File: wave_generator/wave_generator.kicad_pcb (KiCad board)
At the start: 4 copper layers, 100 x 65 mm, 0 parts

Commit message: PCB not finished yet
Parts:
- added C1: 33uF, Capacitor_SMD:CP_Elec_6.3x5.9, F.Cu at (124.5, 72.0)
- added C10: 10uF, Capacitor_SMD:C_0603_1608Metric, F.Cu at (166.2, 73.0)
- added C11: 10uF, Capacitor_SMD:C_0603_1608Metric, F.Cu at (179.2, 74.8)
- added C12: 2.2uF, Capacitor_SMD:C_0603_1608Metric, F.Cu at (181.9, 74.8)
- added C13: 103, Capacitor_SMD:C_0603_1608Metric, F.Cu at (110.7, 96.5)
- added C14: 104, Capacitor_SMD:C_0603_1608Metric, F.Cu at (112.8, 96.5)
- added C15: 104, Capacitor_SMD:C_0603_1608Metric, F.Cu at (130.5, 103.5)
- added C16: 103, Capacitor_SMD:C_0603_1608Metric, F.Cu at (110.7, 110.0)
- added C17: 104, Capacitor_SMD:C_0603_1608Metric, F.Cu at (112.9, 110.0)
- added C18: 104, Capacitor_SMD:C_0603_1608Metric, F.Cu at (130.6, 118.9)
- added C19: 103, Capacitor_SMD:C_0603_1608Metric, F.Cu at (136.6, 103.5)
- added C2: 22uF, Capacitor_SMD:CP_Elec_6.3x5.9, F.Cu at (116.5, 72.0)
- added C20: 103, Capacitor_SMD:C_0603_1608Metric, F.Cu at (137.1, 118.9)
- added C21: 104, Capacitor_SMD:C_0603_1608Metric, F.Cu at (139.8, 100.2)
- added C22: 10pF, Capacitor_SMD:C_0603_1608Metric, F.Cu at (156.1, 100.7)
- added C23: 10pF, Capacitor_SMD:C_0603_1608Metric, F.Cu at (148.4, 100.7)
- added C24: 103, Capacitor_SMD:C_0603_1608Metric, F.Cu at (160.8, 111.8)
- added C25: 104, Capacitor_SMD:C_0603_1608Metric, F.Cu at (162.9, 111.8)
- added C26: 10uF, Capacitor_SMD:C_0603_1608Metric, F.Cu at (165.8, 111.0)
- added C27: 10uF, Capacitor_SMD:C_0603_1608Metric, F.Cu at (175.7, 101.3)
- added C28: 103, Capacitor_SMD:C_0603_1608Metric, F.Cu at (188.4, 113.7)
- added C29: 103, Capacitor_SMD:C_0603_1608Metric, F.Cu at (192.7, 88.9)
- added C3: 33uF, Capacitor_SMD:CP_Elec_6.3x5.9, F.Cu at (151.9, 75.0)
- added C30: 103, Capacitor_SMD:C_0603_1608Metric, F.Cu at (189.1, 89.0)
- added C31: 103, Capacitor_SMD:C_0603_1608Metric, F.Cu at (185.8, 89.0)
- added C32: 103, Capacitor_SMD:C_0603_1608Metric, F.Cu at (182.5, 89.0)
- added C33: 103, Capacitor_SMD:C_0603_1608Metric, F.Cu at (179.3, 89.0)
- added C34: 104, Capacitor_SMD:C_0603_1608Metric, F.Cu at (192.6, 84.1)
- added C35: 104, Capacitor_SMD:C_0603_1608Metric, F.Cu at (188.8, 84.0)
- added C36: 104, Capacitor_SMD:C_0603_1608Metric, F.Cu at (185.6, 84.1)
- added C37: 104, Capacitor_SMD:C_0603_1608Metric, F.Cu at (182.2, 84.1)
- added C38: 104, Capacitor_SMD:C_0603_1608Metric, F.Cu at (179.1, 84.1)
- added C4: 22uF, Capacitor_SMD:CP_Elec_6.3x5.9, F.Cu at (160.4, 75.0)
- added C5: 33uF, Capacitor_SMD:CP_Elec_6.3x5.9, F.Cu at (116.5, 86.5)
- added C6: 22uF, Capacitor_SMD:CP_Elec_6.3x5.9, F.Cu at (124.5, 86.5)
- added C7: 33uF, Capacitor_SMD:CP_Elec_6.3x5.9, F.Cu at (160.5, 86.5)
- added C8: 22uF, Capacitor_SMD:CP_Elec_6.3x5.9, F.Cu at (152.0, 86.5)
- added C9: 2.2uF, Capacitor_SMD:C_0603_1608Metric, F.Cu at (166.2, 77.0)
- added D1: LED_RED, LED_SMD:LED_0603_1608Metric, F.Cu at (184.3, 74.8)
- added D2: LED_BLUE, LED_SMD:LED_0603_1608Metric, F.Cu at (179.9, 128.0)
- added D3: LED_BLUE, LED_SMD:LED_0603_1608Metric, F.Cu at (179.8, 124.7)
- added F1: Fuse, Fuse:Fuse_1206_3216Metric, F.Cu at (111.0, 74.5)
- added F2: Fuse, Fuse:Fuse_1206_3216Metric, F.Cu at (111.0, 87.8)
- added J1: KF301_3PIN_POWER, myfootprint:KF301-3P, F.Cu at (103.2, 85.0)
- added J2: KF301_2PIN_INPUT, myfootprint:KF301-2P, F.Cu at (103.2, 100.0)
- added J3: KF301_2PIN_INPUT, myfootprint:KF301-2P, F.Cu at (103.2, 112.5)
- added J4: KF301_2PIN_OUTPUT, myfootprint:KF301-2P, F.Cu at (196.8, 97.3)
- added J5: UART, Connector_PinHeader_2.54mm:PinHeader_1x04_P2.54mm_Vertical, F.Cu at (167.4, 127.7)
- added J6: SWD, Connector_PinHeader_2.54mm:PinHeader_1x04_P2.54mm_Vertical, F.Cu at (152.2, 127.7)
- added J7: TEST, Connector_PinHeader_2.54mm:PinHeader_1x04_P2.54mm_Vertical, F.Cu at (137.6, 127.6)
- added R1: 200R, Resistor_SMD:R_0603_1608Metric, F.Cu at (114.9, 96.5)
- added R11: 10K, Resistor_SMD:R_0603_1608Metric, F.Cu at (115.1, 118.8)
- added R12: 10K, Resistor_SMD:R_0603_1608Metric, F.Cu at (132.8, 118.9)
- added R13: 30K, Resistor_SMD:R_0603_1608Metric, F.Cu at (134.9, 118.9)
- added R14: 10K, Resistor_SMD:R_0603_1608Metric, F.Cu at (141.2, 114.8)
- added R15: 10K, Resistor_SMD:R_0603_1608Metric, F.Cu at (139.8, 96.2)
- added R16: 1M, Resistor_SMD:R_0603_1608Metric, F.Cu at (152.5, 97.6)
- added R17: 10K, Resistor_SMD:R_0603_1608Metric, F.Cu at (169.4, 111.0)
- added R18: 10K, Resistor_SMD:R_0603_1608Metric, F.Cu at (160.8, 103.2)
- added R19: 10K, Resistor_SMD:R_0603_1608Metric, F.Cu at (175.6, 97.7)
- added R2: 200R, Resistor_SMD:R_0603_1608Metric, F.Cu at (117.0, 96.5)
- added R20: 10K, Resistor_SMD:R_0603_1608Metric, F.Cu at (180.1, 111.0)
- added R21: 30K, Resistor_SMD:R_0603_1608Metric, F.Cu at (184.9, 111.7)
- added R22: 300R, Resistor_SMD:R_0603_1608Metric, F.Cu at (188.4, 111.7)
- added R23: 10K, Resistor_SMD:R_0603_1608Metric, F.Cu at (191.7, 112.8)
- added R24: 3.3K, Resistor_SMD:R_0603_1608Metric, F.Cu at (188.0, 74.5)
- added R25: 3.3K, Resistor_SMD:R_0603_1608Metric, F.Cu at (185.4, 128.0)
- added R26: 3.3K, Resistor_SMD:R_0603_1608Metric, F.Cu at (185.3, 124.7)
- added R3: 10K, Resistor_SMD:R_0603_1608Metric, F.Cu at (117.0, 103.5)
- added R4: 10K, Resistor_SMD:R_0603_1608Metric, F.Cu at (114.9, 103.5)
- added R5: 10K, Resistor_SMD:R_0603_1608Metric, F.Cu at (132.5, 103.5)
- added R6: 30K, Resistor_SMD:R_0603_1608Metric, F.Cu at (134.5, 103.5)
- added R7: 200R, Resistor_SMD:R_0603_1608Metric, F.Cu at (115.1, 110.0)
- added R8: 200R, Resistor_SMD:R_0603_1608Metric, F.Cu at (117.3, 110.0)
- added R9: 10K, Resistor_SMD:R_0603_1608Metric, F.Cu at (117.3, 118.8)
- added RST1: SW_Push, Button_Switch_SMD:SW_SPST_CK_RS282G05A3, F.Cu at (143.3, 97.4)
- added RV1: 20K, myfootprint:R_Potential, F.Cu at (123.5, 97.5)
- added RV2: 20K, myfootprint:R_Potential, F.Cu at (123.5, 113.0)
- added RV3: 20K, myfootprint:R_Potential, F.Cu at (167.4, 96.7)
- added RV4: 20K, myfootprint:R_Potential, F.Cu at (186.0, 96.7)
- added TP1: TestPoint, Connector_Pin:Pin_D0.7mm_L6.5mm_W1.8mm_FlatFork, F.Cu at (134.5, 107.4)
- added TP2: TestPoint, Connector_Pin:Pin_D0.7mm_L6.5mm_W1.8mm_FlatFork, F.Cu at (134.5, 111.4)
- added TP3: TestPoint, Connector_Pin:Pin_D0.7mm_L6.5mm_W1.8mm_FlatFork, F.Cu at (168.6, 115.2)
- added TP4: TestPoint, Connector_Pin:Pin_D0.7mm_L6.5mm_W1.8mm_FlatFork, F.Cu at (176.5, 105.8)
- added TP5: TestPoint, Connector_Pin:Pin_D0.7mm_L6.5mm_W1.8mm_FlatFork, F.Cu at (152.0, 67.0)
- added TP6: TestPoint, Connector_Pin:Pin_D0.7mm_L6.5mm_W1.8mm_FlatFork, F.Cu at (173.0, 67.0)
- added TP7: TestPoint, Connector_Pin:Pin_D0.7mm_L6.5mm_W1.8mm_FlatFork, F.Cu at (167.2, 83.7)
- added U1: L7809, Package_TO_SOT_SMD:TO-263-2, F.Cu at (138.0, 71.5)
- added U2: LM7909, Package_TO_SOT_SMD:TO-263-2, F.Cu at (138.0, 85.5)
- added U3: AMS1117-3.3, Package_TO_SOT_SMD:SOT-223-3_TabPin2, F.Cu at (173.2, 75.4)
- added U4: OP07, Package_SO:SOP-8_3.9x4.9mm_P1.27mm, F.Cu at (123.5, 103.6)
- added U5: OP07, Package_SO:SOP-8_3.9x4.9mm_P1.27mm, F.Cu at (123.5, 119.0)
- added U6: OP07, Package_SO:SOP-8_3.9x4.9mm_P1.27mm, F.Cu at (167.4, 103.0)
- added U7: OP07, Package_SO:SOP-8_3.9x4.9mm_P1.27mm, F.Cu at (186.8, 104.7)
- added U8: STM32F103RCT6, Package_QFP:LQFP-64_10x10mm_P0.5mm, F.Cu at (149.9, 112.3)
- added X1: 16Mhz_Passive_3225, Oscillator:Oscillator_SMD_EuroQuartz_XO32-4Pin_3.2x2.5mm, F.Cu at (152.6, 100.7)

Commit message: Finished PCB
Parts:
- added W1: M3_Whole, myfootprint:M3_Whole, F.Cu at (104.0, 69.0)
- added W2: M3_Whole, myfootprint:M3_Whole, F.Cu at (196.0, 69.0)
- added W3: M3_Whole, myfootprint:M3_Whole, F.Cu at (104.0, 126.0)
- added W4: M3_Whole, myfootprint:M3_Whole, F.Cu at (196.0, 126.0)
- moved C34 62.9 mm to (140.3, 119.2), turned to 180 degrees
- moved C29 59.1 mm to (140.3, 116.2), turned to 180 degrees
- moved C37 46.5 mm to (155.8, 122.2), turned to 180 degrees
- moved C35 44.3 mm to (147.3, 99.7), turned to 0 degrees
- moved C30 43.6 mm to (147.3, 101.5), turned to 0 degrees
- moved C32 41.2 mm to (155.8, 120.4), turned to 180 degrees
- moved J7 40.2 mm to (177.8, 128.0)
- moved C36 38.9 mm to (162.9, 115.7), turned to -90 degrees
- moved C31 36.6 mm to (160.8, 115.7), turned to -90 degrees
- moved R16 26.5 mm to (148.2, 123.8), turned to 180 degrees
- moved C38 26.0 mm to (158.2, 99.5), turned to 0 degrees
- moved C33 24.6 mm to (158.2, 101.5), turned to 0 degrees
- moved C22 23.2 mm to (145.2, 121.2), turned to 90 degrees
- moved X1 20.9 mm to (148.2, 121.2), turned to -90 degrees
- moved C23 20.6 mm to (151.4, 121.2), turned to -90 degrees
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- renumbered D2 to amp, D3 to freq, D1 to power
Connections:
- C27 pad 1: /Amplitude -> /OUT_TEMP
- J5 pad 2: /UART_RX -> /USART_TX
- J5 pad 3: /UART_TX -> /USART_RX
- R18 pad 1: /Amplitude -> /OUT_TEMP
- TP4 pad 1: /Amplitude -> /OUT_TEMP
- U6 pad 6: /Amplitude -> /OUT_TEMP
- U8 pad 16: unconnected-(U8-Pad16) -> /USART_TX
- U8 pad 17: unconnected-(U8-Pad17) -> /USART_RX
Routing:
- net GND: track 0.00 -> 568.7 mm, vias 0 -> 191
- net +9V: track 0.00 -> 225.9 mm
- net +3V3: track 0.00 -> 196.7 mm, vias 0 -> 10
- net -9V: track 0.00 -> 98.4 mm, vias 0 -> 2
- net /PA6: track 0.00 -> 52.2 mm, vias 0 -> 1
- net /PA8: track 0.00 -> 52.0 mm, vias 0 -> 1
- net /PA7: track 0.00 -> 46.2 mm, vias 0 -> 1
- net /SWCLK: track 0.00 -> 42.4 mm, vias 0 -> 1
- net /DAC_OUT2: track 0.00 -> 38.7 mm, vias 0 -> 2
- net Net-(C1-Pad1): track 0.00 -> 38.4 mm
- net Net-(C20-Pad1): track 0.00 -> 36.3 mm, vias 0 -> 1
- net Net-(C19-Pad1): track 0.00 -> 30.6 mm, vias 0 -> 1
- net /Freq_LED: track 0.00 -> 30.4 mm, vias 0 -> 2
- net /Amp_LED: track 0.00 -> 30.1 mm, vias 0 -> 2
- net Net-(C5-Pad2): track 0.00 -> 26.0 mm
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- added copper zone on B.Cu, net GND
- added copper zone on F.Cu, net GND
- added copper zone on In1.Cu, net GND
- added copper zone on In2.Cu, net GND
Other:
- outline, holes or cut-outs redrawn
- board text added: "+15V"
- board text added: "-15V"
- board text added: "3V3"
- board text added: "Amp_In"
- board text added: "CLK"
- board text added: "DAC_OUT2"
- board text added: "DIO"
- board text added: "Freq_In"
- board text added: "GND"
- board text added: "OUTPUT"
- board text added: "PA6"
- board text added: "PA7"
- board text added: "PA8"
- board text added: "U2_RX"
- board text added: "U2_TX"
- board text added: "Wave Generator Designed By Jeffrey 2022-4-10"

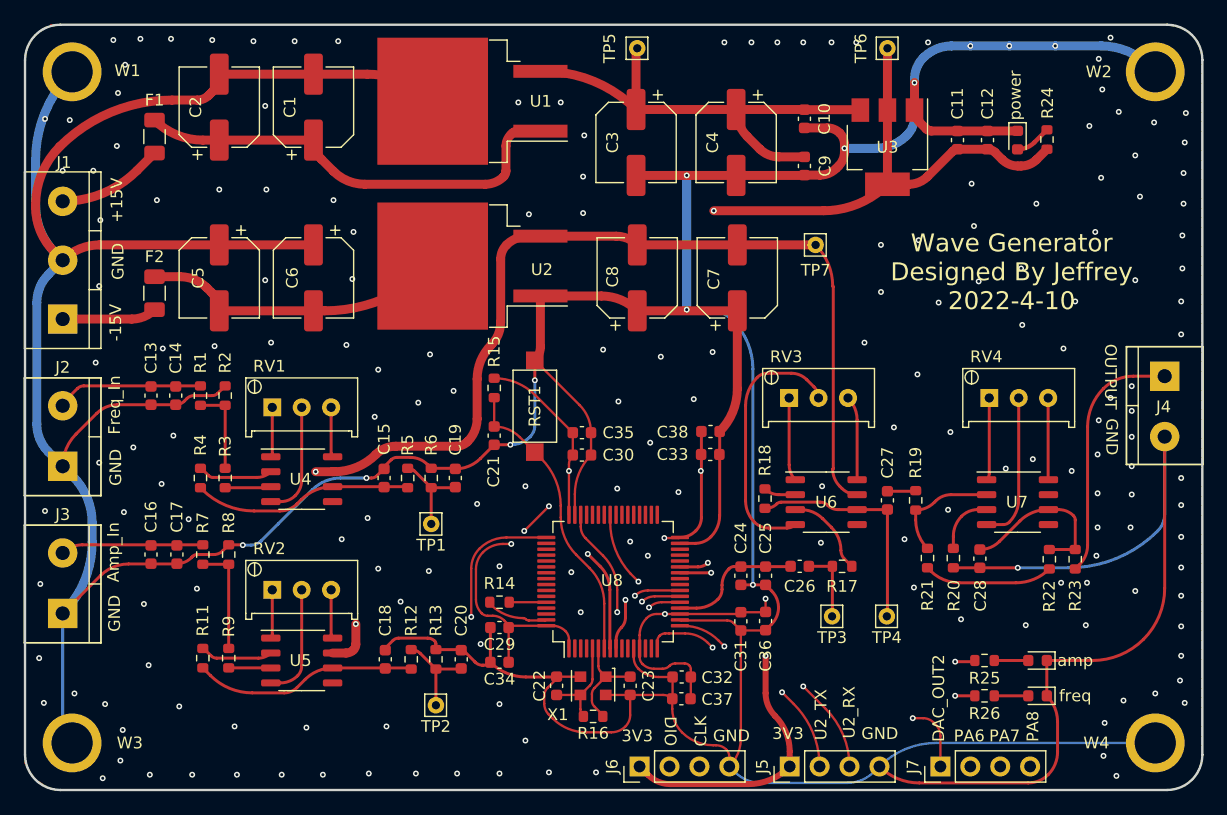
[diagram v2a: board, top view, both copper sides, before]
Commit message: fixed hardware error
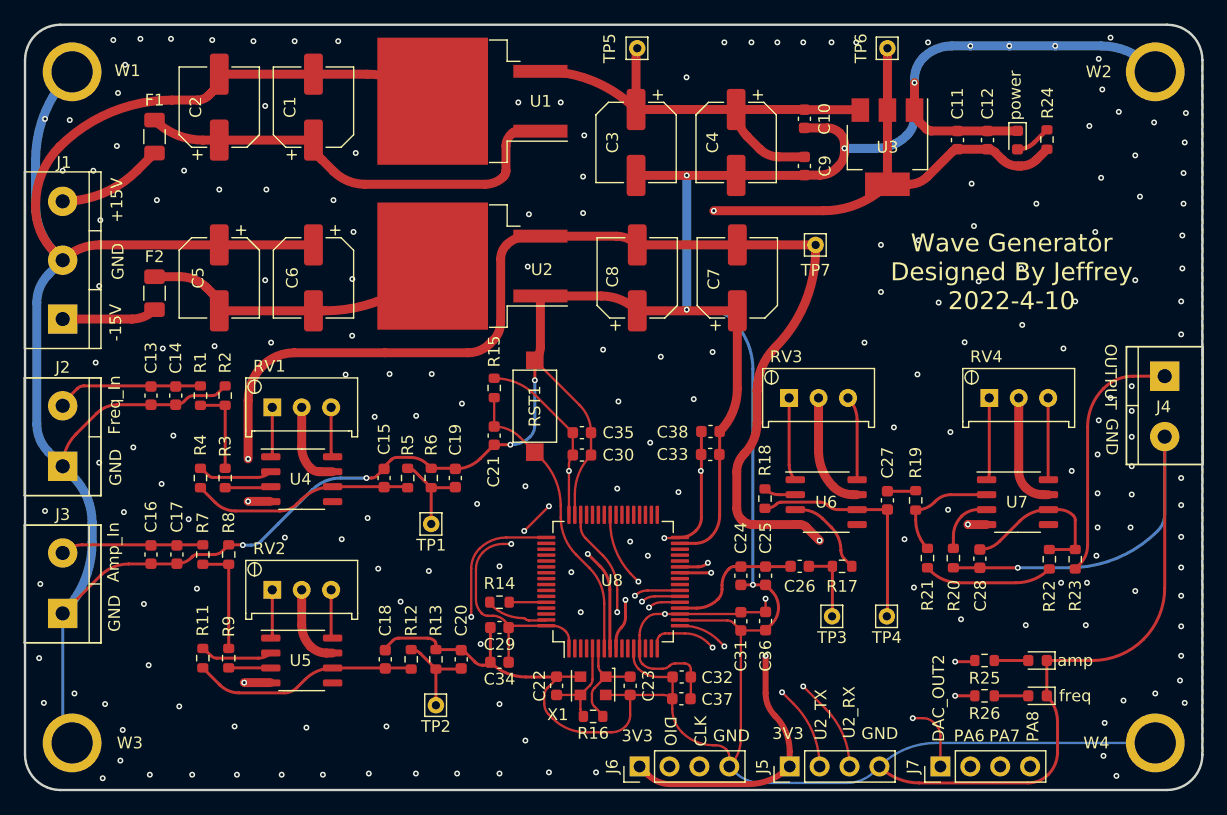
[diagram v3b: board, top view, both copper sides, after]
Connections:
- U4 pad 4: +9V -> -9V
- U4 pad 7: -9V -> +9V
- U5 pad 4: +9V -> -9V
- U5 pad 7: -9V -> +9V
- U6 pad 4: +9V -> -9V
- U6 pad 7: -9V -> +9V
- U7 pad 4: +9V -> -9V
- U7 pad 7: -9V -> +9V
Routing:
- net -9V: track 98.4 -> 134.1 mm, vias 2 -> 5
- net +9V: track 225.9 -> 205.0 mm
- net GND: vias 191 -> 194

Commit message: new version V2.0
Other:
- board text added: "Wave Generator V2.0 Designed By Jeffrey 2022-4-20"
- board text removed: "Wave Generator Designed By Jeffrey 2022-4-10"
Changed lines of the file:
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@@
       (drillshape 0)
       (scaleselection 1)
-      (outputdirectory "wave_generator_V1.0/")
+      (outputdirectory "wave_generator_V1.1/")
     )
   )
@@
     (effects (font (size 1 1) (thickness 0.15)))
   )
-  (gr_text "Wave Generator\nDesigned By Jeffrey\n2022-4-10" (at 183.8 86) (layer "F.SilkS")
+  (gr_text "Wave Generator V2.0\nDesigned By Jeffrey\n2022-4-20" (at 183.799988 86.000006) (layer "F.SilkS")
     (effects (font (size 1.524 1.524) (thickness 0.254)))
   )
